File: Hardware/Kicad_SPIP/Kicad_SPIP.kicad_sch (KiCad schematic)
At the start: 20 parts, among them J1 Conn_01x03, J2 Conn_01x02, J3 Conn_01x04, J4 Conn_01x06, J5 Conn_01x06, J6 Conn_01x06, U1 STM32G431CBUx, U3 DRV8411APWPR

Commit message: Nouvelle version du Kicad
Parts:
- removed D1: 1N4148WT, Diode_SMD:D_SOD-523, symbol Diode:1N4148WT
- R1: value 10kOhm -> 330 Ohm
- R2: value 10kOhm -> 1kOhm
- R3, R4: value 33kOhm -> 82kOhm
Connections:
- net +3.3V: no longer R1.2
- net DATA: now also R1.2; no longer R1.1, U1.31 (PA9)
- net LEFT_ENC_A: now also U1.30 (PA8); no longer U1.42 (PB4)
- net LEFT_ENC_B: now also U1.31 (PA9); no longer U1.43 (PB5)
- net X1: now also J4.2 (Pin_2), U1.12 (PA4); no longer J4.5 (Pin_5), U1.16 (PC4)
- net X2: now also J4.3 (Pin_3), U1.13 (PA5); no longer J4.4 (Pin_4), U1.2 (PC13)
- net X3: now also J4.4 (Pin_4), U1.14 (PA6); no longer J4.3 (Pin_3), U1.3 (PC14)
- net X4: now also J4.5 (Pin_5), U1.15 (PA7); no longer J4.2 (Pin_2), U1.4 (PC15)
- net AIN1: now reaches U1.33 (PA11)
- net AIN1: now also U3.16 (AIN1)
- net AIN2: now reaches U1.34 (PA12)
- net AIN2: now also U3.15 (AIN2)
- removed net IN1: U1.15 (PA7), U3.16 (AIN1)
- removed net IN2: U1.14 (PA6), U3.15 (AIN2)
- net IN3 renamed BIN1
- net BIN1: now also U1.10 (PA2); no longer U1.11 (PA3)
- net IN4 renamed BIN2
- net BIN2: now also U1.11 (PA3); no longer U1.10 (PA2)
- net OUT1 renamed AOUT1
- net OUT2 renamed AOUT2
- net OUT3 renamed BOUT1
- net OUT4 renamed BOUT2
- new net: R1.1, U1.16 (PC4)
- no-connect marks 25 -> 23
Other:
- moved on the sheet: C3, C4, C5, R1

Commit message: rajout fichier des composants et des empreintes
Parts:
- C1, C6: footprint (none) -> Capacitor_SMD:C_0603_1608Metric
- C2, C3, C4, C5, C7: footprint (none) -> Capacitor_SMD:C_0402_1005Metric
- J1: footprint (none) -> Connector_JST:JST_XH_B3B-XH-A_1x03_P2.50mm_Vertical
- J2: footprint (none) -> Connector_JST:JST_XH_B2B-XH-A_1x02_P2.50mm_Vertical
- J3: footprint (none) -> Connector_JST:JST_XH_B4B-XH-A_1x04_P2.50mm_Vertical
- J4, J5, J6: footprint (none) -> Connector_JST:JST_XH_B6B-XH-A_1x06_P2.50mm_Vertical
- R1, R4: footprint (none) -> Resistor_SMD:R_0805_2012Metric
- R2: footprint (none) -> Resistor_SMD:R_0402_1005Metric
- R3: value 82kOhm -> 82.5kOhm; footprint (none) -> Resistor_SMD:R_0805_2012Metric
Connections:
- no-connect marks 23 -> 26
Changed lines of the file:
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@@
 	)
 	(no_connect
+		(at 45.72 76.2)
+	)
+	(no_connect
 		(at 45.72 58.42)
 	)
@@
 	)
 	(no_connect
+		(at 45.72 78.74)
+	)
+	(no_connect
 		(at 45.72 114.3)
 	)
@@
 	)
 	(no_connect
+		(at 45.72 81.28)
+	)
+	(no_connect
 		(at 45.72 116.84)
 	)
@@
 			)
 		)
-		(property "Footprint" ""
+		(property "Footprint" "Connector_JST:JST_XH_B6B-XH-A_1x06_P2.50mm_Vertical"
 			(at 214.63 68.58 0)
 			(effects
@@
 			)
 		)
-		(property "Footprint" ""
+		(property "Footprint" "Capacitor_SMD:C_0402_1005Metric"
 			(at 180.34 34.29 0)
 			(effects
@@
 			)
 		)
-		(property "Footprint" ""
+		(property "Footprint" "Connector_JST:JST_XH_B6B-XH-A_1x06_P2.50mm_Vertical"
 			(at 262.89 100.33 0)
 			(effects
@@
 			)
 		)
-		(property "Footprint" ""
+		(property "Footprint" "Capacitor_SMD:C_0402_1005Metric"
 			(at 76.2 33.02 0)
 			(effects
@@
 			)
 		)
-		(property "Footprint" ""
+		(property "Footprint" "Capacitor_SMD:C_0402_1005Metric"
 			(at 55.88 33.02 0)
 			(effects
@@
 			)
 		)
-		(property "Footprint" ""
+		(property "Footprint" "Resistor_SMD:R_0805_2012Metric"
 			(at 175.26 54.61 0)
 			(effects
@@
 			)
 		)
-		(property "Footprint" ""
+		(property "Footprint" "Capacitor_SMD:C_0402_1005Metric"
 			(at 63.5 33.02 0)
 			(effects
@@
 			)
 		)
-		(property "Footprint" ""
+		(property "Footprint" "Connector_JST:JST_XH_B4B-XH-A_1x04_P2.50mm_Vertical"
 			(at 261.62 34.29 0)
 			(effects
@@
 			)
 		)
-		(property "Value" "82kOhm"
+		(property "Value" "82.5kOhm"
 			(at 173.99 67.3099 0)
 			(effects
@@
 			)
 		)
-		(property "Footprint" ""
+		(property "Footprint" "Resistor_SMD:R_0805_2012Metric"
 			(at 171.45 66.04 0)
 			(effects
@@
 			)
 		)
-		(property "Footprint" ""
+		(property "Footprint" "Connector_JST:JST_XH_B6B-XH-A_1x06_P2.50mm_Vertical"
 			(at 214.63 34.29 0)
 			(effects
@@
 			)
 		)
-		(property "Footprint" ""
+		(property "Footprint" "Resistor_SMD:R_0805_2012Metric"
 			(at 34.29 66.04 0)
 			(effects
@@
 			)
 		)
-		(property "Footprint" ""
+		(property "Footprint" "Capacitor_SMD:C_0603_1608Metric"
 			(at 172.72 34.29 0)
 			(effects
@@
 			)
 		)
-		(property "Footprint" ""
+		(property "Footprint" "Capacitor_SMD:C_0603_1608Metric"
 			(at 68.58 33.02 0)
 			(effects
@@
 			)
 		)
-		(property "Footprint" ""
+		(property "Footprint" "Capacitor_SMD:C_0402_1005Metric"
 			(at 48.26 33.02 0)
 			(effects
@@
 			)
 		)
-		(property "Footprint" ""
+		(property "Footprint" "Connector_JST:JST_XH_B2B-XH-A_1x02_P2.50mm_Vertical"
 			(at 261.62 68.58 0)
 			(effects
@@
 			)
 		)
-		(property "Footprint" ""
+		(property "Footprint" "Connector_JST:JST_XH_B3B-XH-A_1x03_P2.50mm_Vertical"
 			(at 149.86 100.33 0)
 			(effects
@@
 			)
 		)
-		(property "Footprint" ""
+		(property "Footprint" "Resistor_SMD:R_0402_1005Metric"
 			(at 179.07 44.45 0)
 			(effects

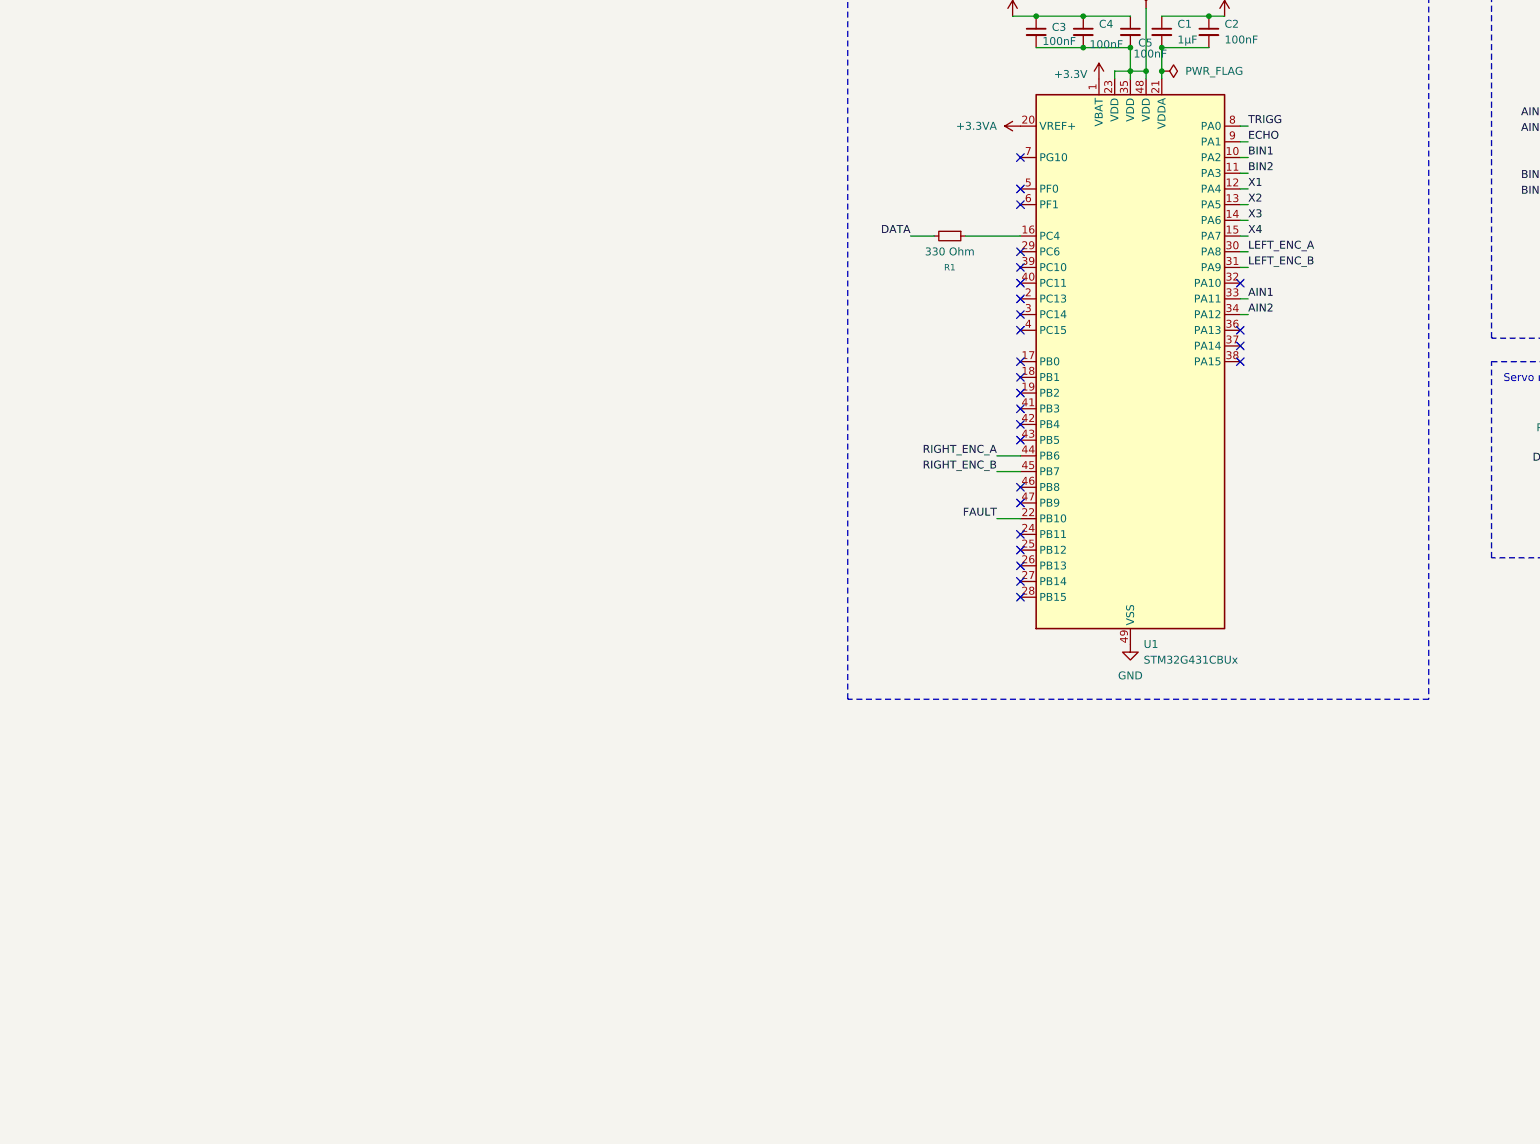
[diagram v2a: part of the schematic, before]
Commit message: mise à jour de la schématique du PCB
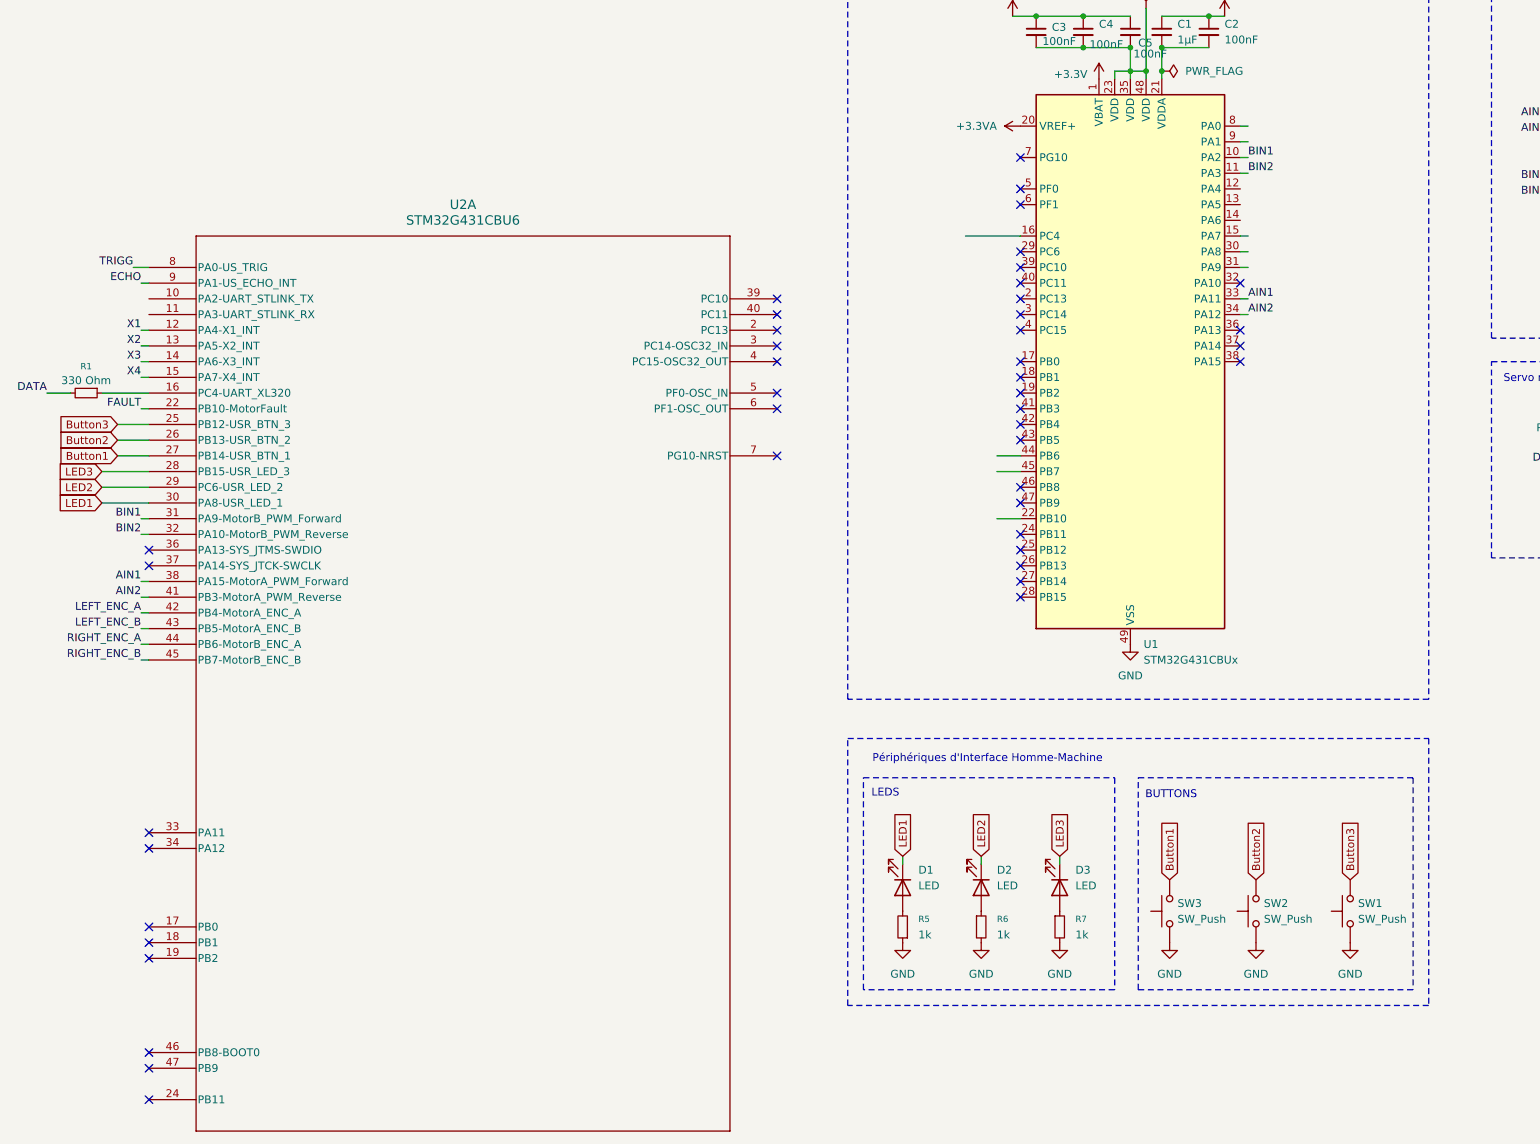
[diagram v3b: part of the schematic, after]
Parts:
- added D1, D2, D3: LED, symbol Device:LED
- added R5, R6, R7: 1k, symbol Device:R_Small
- added SW1, SW2, SW3: SW_Push, symbol Switch:SW_Push
- added U2: STM32G431CBU6, UFQFPN-48_7X7X0P55MM, symbol STM32G431CBU6_SPIP:STM32G431CBU6
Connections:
- net AIN1: now also U2.38 (PA15-MotorA_PWM_Forward)
- net AIN2: now also U2.41 (PB3-MotorA_PWM_Reverse)
- net BIN1: now also U2.31 (PA9-MotorB_PWM_Forward)
- net BIN2: now also U2.32 (PA10-MotorB_PWM_Reverse)
- net ECHO: now also U2.9 (PA1-US_ECHO_INT); no longer U1.9 (PA1)
- net FAULT: now also U2.22 (PB10-MotorFault); no longer U1.22 (PB10)
- net GND: now also R5.1, R6.2, R7.2, SW1.1, SW2.1, SW3.1
- net LEFT_ENC_A: now also U2.42 (PB4-MotorA_ENC_A); no longer U1.30 (PA8)
- net LEFT_ENC_B: now also U2.43 (PB5-MotorA_ENC_B); no longer U1.31 (PA9)
- net RIGHT_ENC_A: now also U2.44 (PB6-MotorB_ENC_A); no longer U1.44 (PB6)
- net RIGHT_ENC_B: now also U2.45 (PB7-MotorB_ENC_B); no longer U1.45 (PB7)
- net TRIGG: now also U2.8 (PA0-US_TRIG); no longer U1.8 (PA0)
- net X1: now also U2.12 (PA4-X1_INT); no longer U1.12 (PA4)
- net X2: now also U2.13 (PA5-X2_INT); no longer U1.13 (PA5)
- net X3: now also U2.14 (PA6-X3_INT); no longer U1.14 (PA6)
- net X4: now also U2.15 (PA7-X4_INT); no longer U1.15 (PA7)
- net at U1.16 (PC4): no longer R1.1
- new net: D2.2 (A), R6.1
- new net: D3.2 (A), R7.1
- new net: R1.1, U2.16 (PC4-UART_XL320)
- new net: D1.2 (A), R5.2
- new net Button1: SW3.2, U2.27 (PB14-USR_BTN_1)
- new net Button2: SW2.2, U2.26 (PB13-USR_BTN_2)
- new net Button3: SW1.2, U2.25 (PB12-USR_BTN_3)
- new net LED1: D1.1 (K), U2.30 (PA8-USR_LED_1)
- new net LED2: D2.1 (K), U2.29 (PC6-USR_LED_2)
- new net LED3: D3.1 (K), U2.28 (PB15-USR_LED_3)
- no-connect marks 26 -> 44
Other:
- note added: "BUTTONS"
- note added: "LEDS"
- note added: "Périphériques d'Interface Homme-Machine"
- moved on the sheet: R1

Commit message: pcb 1.2
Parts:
- removed SW2: SW_Push, symbol Switch:SW_Push
- removed U1: STM32G431CBUx, Package_DFN_QFN:QFN-48-1EP_7x7mm_P0.5mm_EP5.6x5.6mm, symbol MCU_ST_STM32G4:STM32G431CBUx
- removed U3: DRV8411APWPR, DRV8411APWPR:IC_DRV8411APWPR, symbol DRV8411A:DRV8411APWPR
- added C10, C14, C15, C16, C8: 1u, Capacitor_SMD:C_0603_1608Metric, symbol Device:C_Small
- added C11: 10u, Capacitor_SMD:CP_Elec_4x5.4, symbol Device:C_Polarized_Small
- added C13, C9: 10n, Capacitor_SMD:C_0402_1005Metric, symbol Device:C_Small
- added C17: 10n, LED_SMD:LED_0603_1608Metric, symbol Device:C_Small
- added C7: 22u, Capacitor_SMD:C_0805_2012Metric, symbol Device:C_Small
- added D1, D2: LED, LED_SMD:LED_0603_1608Metric, symbol Device:LED
- added H1, H2, H3, H4, H5, H6, H7, H8: MountingHole_Pad, MountingHole:MountingHole_3.2mm_M3_Pad_Via, symbol Mechanical:MountingHole_Pad
- added J2: Conn_ST_STDC14, Connector_PinHeader_1.27mm:PinHeader_2x07_P1.27mm_Vertical_SMD, symbol Connector:Conn_ST_STDC14
- added R12, R14, R15, R16, R2, R8, R9: 10k, Resistor_SMD:R_0402_1005Metric, symbol Device:R_Small
- added R3: 4k3, Resistor_SMD:R_0402_1005Metric, symbol Device:R_Small
- added R4: 1k6, Resistor_SMD:R_0402_1005Metric, symbol Device:R_Small
- added SW1, SW4: SW_Push, Button_Switch_SMD:SW_SPST_B3U-3000P, symbol Switch:SW_Push
- added unit 2 of U1
- added U2: AZ1117CH-3.3TRG1, Package_TO_SOT_SMD:SOT-223-3_TabPin2, symbol Regulator_Linear:AZ1117-3.3
- added U3: DRV8411APWPR, DRV8411APWPR:IC_DRV8411APWPR, symbol DRV8411APWPR:DRV8411APWPR
- C1: value 1µF -> 10u
- C12: renamed from C7; value 100nF -> 100n
- C2, C4, C5: value 100nF -> 100n
- C3: value 100nF -> 10u; footprint Capacitor_SMD:C_0402_1005Metric -> Capacitor_SMD:C_0603_1608Metric
- C6: value 1µF -> 100n; footprint Capacitor_SMD:C_0603_1608Metric -> Capacitor_SMD:C_0402_1005Metric
- D3: renamed from D1; footprint (none) -> LED_SMD:LED_0603_1608Metric; MPN (none) -> 150060BS55040
- D4: renamed from D2; footprint (none) -> LED_SMD:LED_0603_1608Metric; MPN (none) -> 150060GS55040
- D5: renamed from D3; footprint (none) -> LED_SMD:LED_0603_1608Metric; MPN (none) -> 150060RS55040
- J3: renamed from J1; footprint Connector_JST:JST_XH_B3B-XH-A_1x03_P2.50mm_Vertical -> Connector_JST:JST_PH_B3B-PH-K_1x03_P2.00mm_Vertical
- J4: renamed from J3; footprint Connector_JST:JST_XH_B4B-XH-A_1x04_P2.50mm_Vertical -> Connector_JST:JST_PH_B3B-PH-K_1x03_P2.00mm_Vertical
- J5: renamed from J4; footprint Connector_JST:JST_XH_B6B-XH-A_1x06_P2.50mm_Vertical -> Connector_JST:JST_PH_B3B-PH-K_1x03_P2.00mm_Vertical
- J6: renamed from J5; footprint Connector_JST:JST_XH_B6B-XH-A_1x06_P2.50mm_Vertical -> Connector_JST:JST_PH_B6B-PH-K_1x06_P2.00mm_Vertical
- J7: renamed from J6; footprint Connector_JST:JST_XH_B6B-XH-A_1x06_P2.50mm_Vertical -> Connector_JST:JST_PH_B6B-PH-K_1x06_P2.00mm_Vertical
- R1: value 330 Ohm -> 330; footprint Resistor_SMD:R_0805_2012Metric -> Resistor_SMD:R_0402_1005Metric
- R10: renamed from R3; value 82.5kOhm -> 82k5; footprint Resistor_SMD:R_0805_2012Metric -> Resistor_SMD:R_0402_1005Metric
- R11: renamed from R4; value 82kOhm -> 82k5; footprint Resistor_SMD:R_0805_2012Metric -> Resistor_SMD:R_0402_1005Metric
- R13: renamed from R2; value 1kOhm -> 1k
- R5: value 1k -> 680; footprint (none) -> Resistor_SMD:R_0402_1005Metric
- R6: footprint (none) -> Resistor_SMD:R_0402_1005Metric
- R7: value 1k -> 1k6; footprint (none) -> Resistor_SMD:R_0402_1005Metric
- SW2: renamed from SW1; footprint (none) -> Button_Switch_SMD:SW_SPST_B3U-3000P
- SW3: footprint (none) -> Button_Switch_SMD:SW_SPST_B3U-3000P
- U1: renamed from U2; footprint UFQFPN-48_7X7X0P55MM -> STM32G431CBU6:UFQFPN-48_7X7X0P55MM
- renumbered J2 to J1
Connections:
- net +3.3VA is gone; now on net +3.3V: C1.1, C2.1
- net +7.5V is gone; now on net +6V: J3.2 (Pin_2)
- net +3.3V: now also C6.1, C10.1, C14.1, C15.2, C16.2, C7.1, J2.3 (VCC), R14.1, R16.1, R4.2, R9.1, U1.1 (VBAT), U1.20 (VREF+), U1.21 (VDDA), U1.23 (VDD), U1.35 (VDD), U1.48 (VDD), U2.2 (VO), U3.1 (VREF); no longer C3.1
- net +6V: now also C12.1, C3.1, J1.2 (Pin_2), C11.1, C8.2, R3.2, U2.3 (VI), U3.12 (VM); no longer J1.1 (Pin_1)
- net AIN1: now also U3.16 (AIN1)
- net AIN2: now also U3.15 (AIN2)
- net AOUT1: now also U3.2 (AOUT1)
- net AOUT2: now also U3.4 (AOUT2)
- net BIN1: now also U3.9 (BIN1)
- net BIN2: now also U3.10 (BIN2)
- net BOUT1: now also U3.7 (BOUT1)
- net BOUT2: now also U3.5 (BOUT2)
- net Button1: now also C9.2, R8.1; no longer SW3.2
- net Button2: now also C13.2, R12.1
- net Button3: now also C17.2, R15.1; no longer SW2.2
- net FAULT: now also U3.8 (~{FAULT})
- net GND: now also C1.2, C12.2, C2.2, C3.2, C4.2, C5.2, C6.2, D3.1 (K), D4.1 (K), D5.1 (K), J1.1 (Pin_1), C10.2, C11.2, C13.1, C14.2, C15.1, C16.1, C17.1, C7.2, C8.1, C9.1, D1.1 (K), D2.1 (K), H1.1, H2.1, H3.1, H4.1, H5.1, H6.1, H7.1, H8.1, J2.11 (GNDDetect), J2.5 (GND), J2.7 (GND), R2.2, SW1.1, SW4.1, U1.49 (EPAD), U2.1 (GND), U3.13 (GND), U3.17 (EXP), U3.3 (PGNDA), U3.6 (PGNDB); no longer J1.2 (Pin_2), R5.1, R6.2, R7.2
- net at R11.1: now also U3.14 (AIPROPI)
- net STLINK_TX: now reaches U1.10 (PA2-UART_STLINK_TX)
- net STLINK_TX: now also J2.14 (VCP_TX)
- net STLINK_RX: now reaches U1.11 (PA3-UART_STLINK_RX)
- net STLINK_RX: now also J2.13 (VCP_RX)
- net JTMS/SWDIO: now reaches U1.36 (PA13-SYS_JTMS-SWDIO)
- net JTMS/SWDIO: now also J2.4 (JTMS/SWDIO)
- net JCLK/SWCLK: now reaches U1.37 (PA14-SYS_JTCK-SWCLK)
- net JCLK/SWCLK: now also J2.6 (JCLK/SWCLK)
- net at U1.46 (PB8-BOOT0): now also R2.1
- net NRST: now reaches U1.7 (PG10-NRST)
- net NRST: now also J2.12 (~{RST}), SW1.2
- net at R10.1: now also U3.11 (BIPROPI)
- removed net +8V: C12.1, C6.1
- net LED1 renamed LEDB
- net LEDB: now also R5.1; no longer D3.1 (K)
- net LED2 renamed LEDG
- net LEDG: now also R6.2; no longer D4.1 (K)
- net LED3 renamed LEDR
- net LEDR: now also R7.2; no longer D5.1 (K)
- new net: R15.2, R16.2, SW4.2
- new net: R12.2, R14.2, SW3.2
- new net: R8.2, R9.2, SW2.2
- new net: D1.2 (A), R3.1
- new net: D2.2 (A), R4.1
- no-connect marks 44 -> 17
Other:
- note added: "1.7V @ 1mA"
- note added: "2.3V @ 1mA"
- note added: "2.6V @ 1mA"
- note added: "Motor specification Vnom = 6V 300rpm max Istall = 200mA InoLoad = 45mA"
- note added: "MountingHole_Pad"
- note added: "Programmateur"
- moved on the sheet: C12, D3, D4, D5, J1, J3, J4, J5, J6, J7, R1, R10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

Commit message: pcb rootage
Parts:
- removed H5, H6, H7, H8: MountingHole_Pad, MountingHole:MountingHole_3.2mm_M3_Pad_Via, symbol Mechanical:MountingHole_Pad
- C17: footprint LED_SMD:LED_0603_1608Metric -> Capacitor_SMD:C_0402_1005Metric
- J4: footprint Connector_JST:JST_PH_B3B-PH-K_1x03_P2.00mm_Vertical -> Connector_JST:JST_PH_B4B-PH-K_1x04_P2.00mm_Vertical
- J5: footprint Connector_JST:JST_PH_B3B-PH-K_1x03_P2.00mm_Vertical -> Connector_JST:JST_PH_B6B-PH-K_1x06_P2.00mm_Vertical
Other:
- moved on the sheet: H1, H2, H3, H4
